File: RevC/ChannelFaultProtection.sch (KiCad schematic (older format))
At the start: 1 part

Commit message: updates
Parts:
- U_LOAD2: LcscNo (none) -> C100028
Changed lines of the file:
@@
 $Descr A4 11693 8268
 encoding utf-8
-Sheet 11 29
+Sheet 15 29
 Title ""
 Date ""
@@
 AR Path="/5DF46F3E/5DF57DA8" Ref="U_LOAD8"  Part="1"
 AR Path="/5DF61078/5DF57DA8" Ref="U_LOAD9"  Part="1"
-F 0 "U_LOAD9" H 5950 2677 50  0000 C CNN
+F 0 "U_LOAD5" H 5950 2677 50  0000 C CNN
 F 1 "NCV8450" H 5950 2586 50  0000 C CNN
 F 2 "Package_TO_SOT_SMD:SOT-223-3_TabPin2" H 5950 2700 50  0001 C CNN
-F 3 "" H 5950 3100 50  0001 C CNN
+F 3 "https://datasheet.lcsc.com/szlcsc/1912111437_ON-Semiconductor-NCV8450ASTT3G_C100028.pdf" H 5950 3100 50  0001 C CNN
+F 4 "C100028" H 5950 2950 50  0001 C CNN "LcscNo"
 	1    5950 2950
 	1    0    0    -1

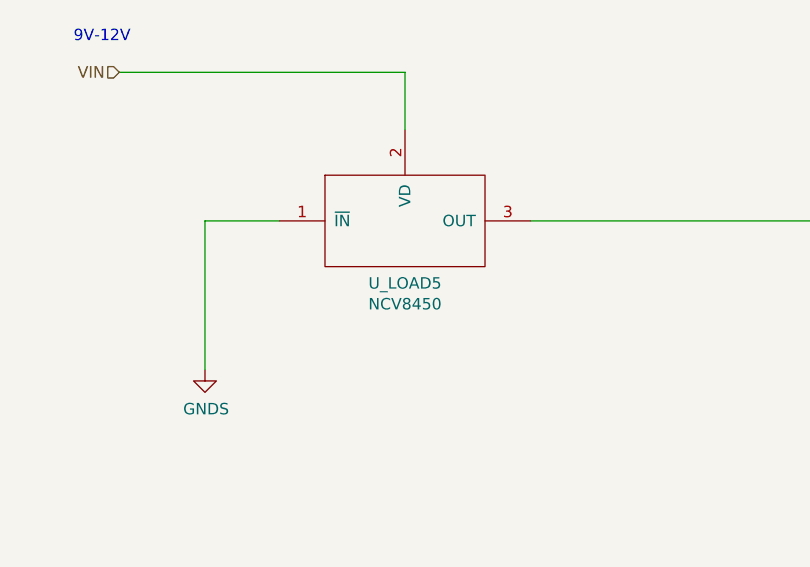
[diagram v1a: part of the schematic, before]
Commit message: Replaced 6N135 SMDIP8 with H11L1 SMDIP6
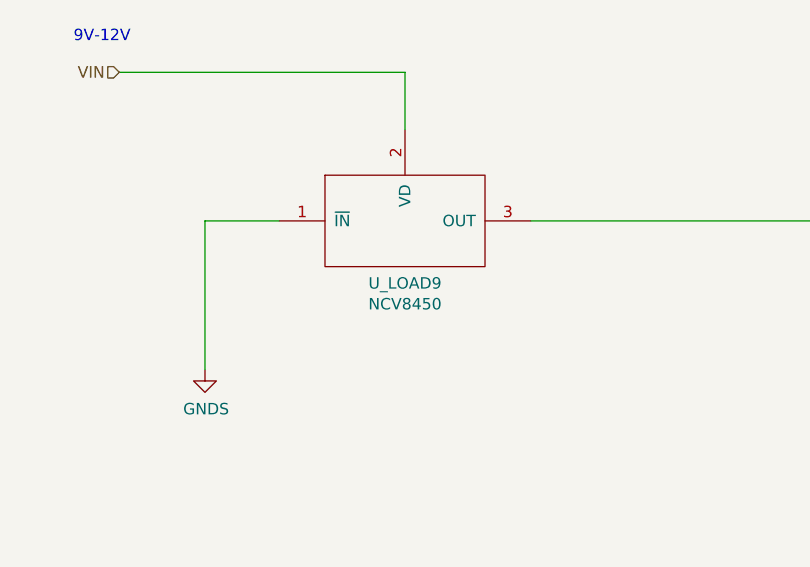
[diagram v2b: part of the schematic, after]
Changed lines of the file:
@@
 AR Path="/5DF46F3E/5DF57DA8" Ref="U_LOAD8"  Part="1"
 AR Path="/5DF61078/5DF57DA8" Ref="U_LOAD9"  Part="1"
-F 0 "U_LOAD5" H 5950 2677 50  0000 C CNN
+F 0 "U_LOAD9" H 5950 2677 50  0000 C CNN
 F 1 "NCV8450" H 5950 2586 50  0000 C CNN
 F 2 "Package_TO_SOT_SMD:SOT-223-3_TabPin2" H 5950 2700 50  0001 C CNN
